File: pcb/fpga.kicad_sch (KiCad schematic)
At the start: 0 parts

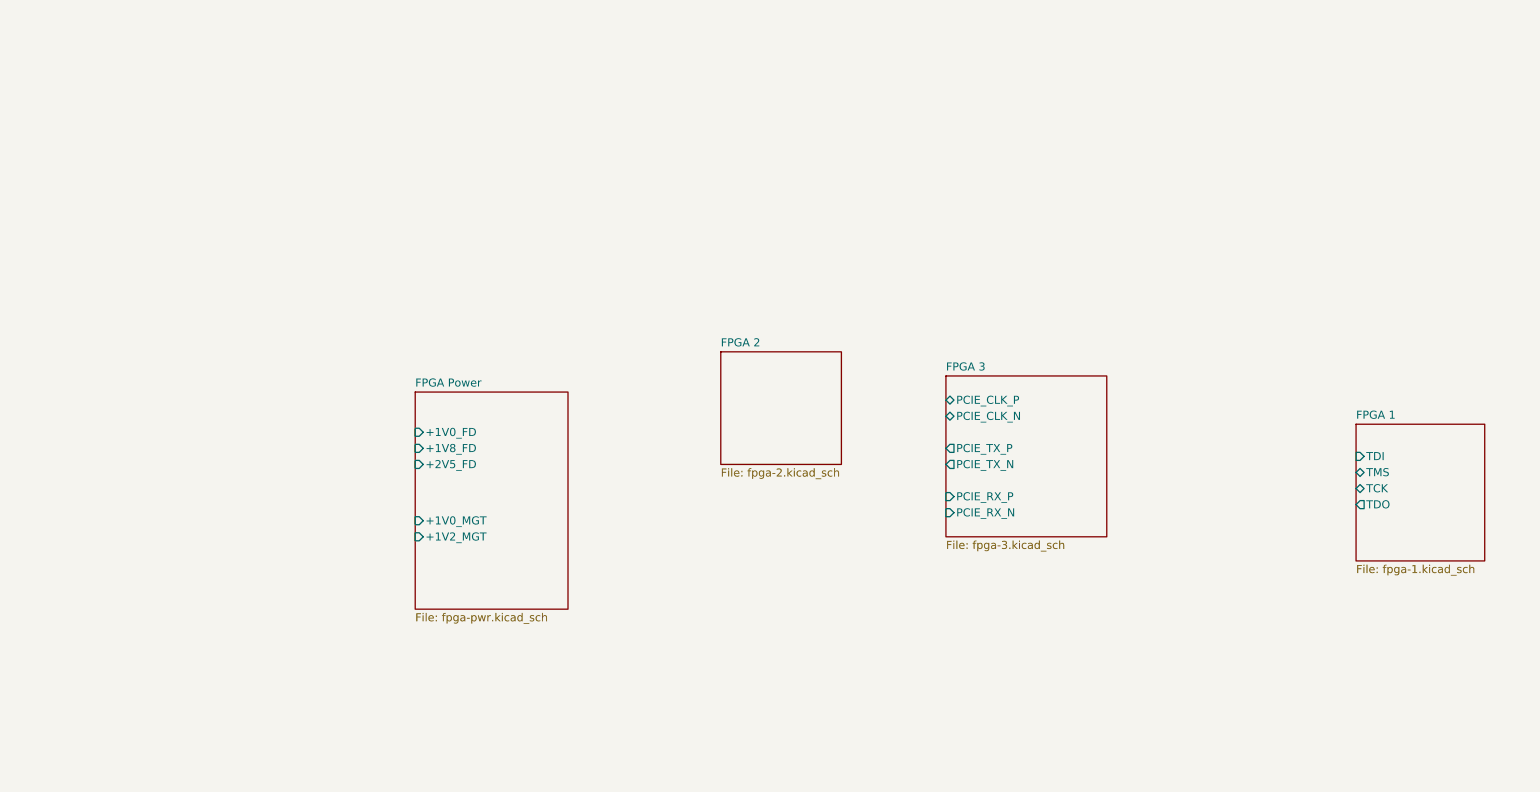
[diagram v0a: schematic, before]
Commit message: completed bus aliasing definitions
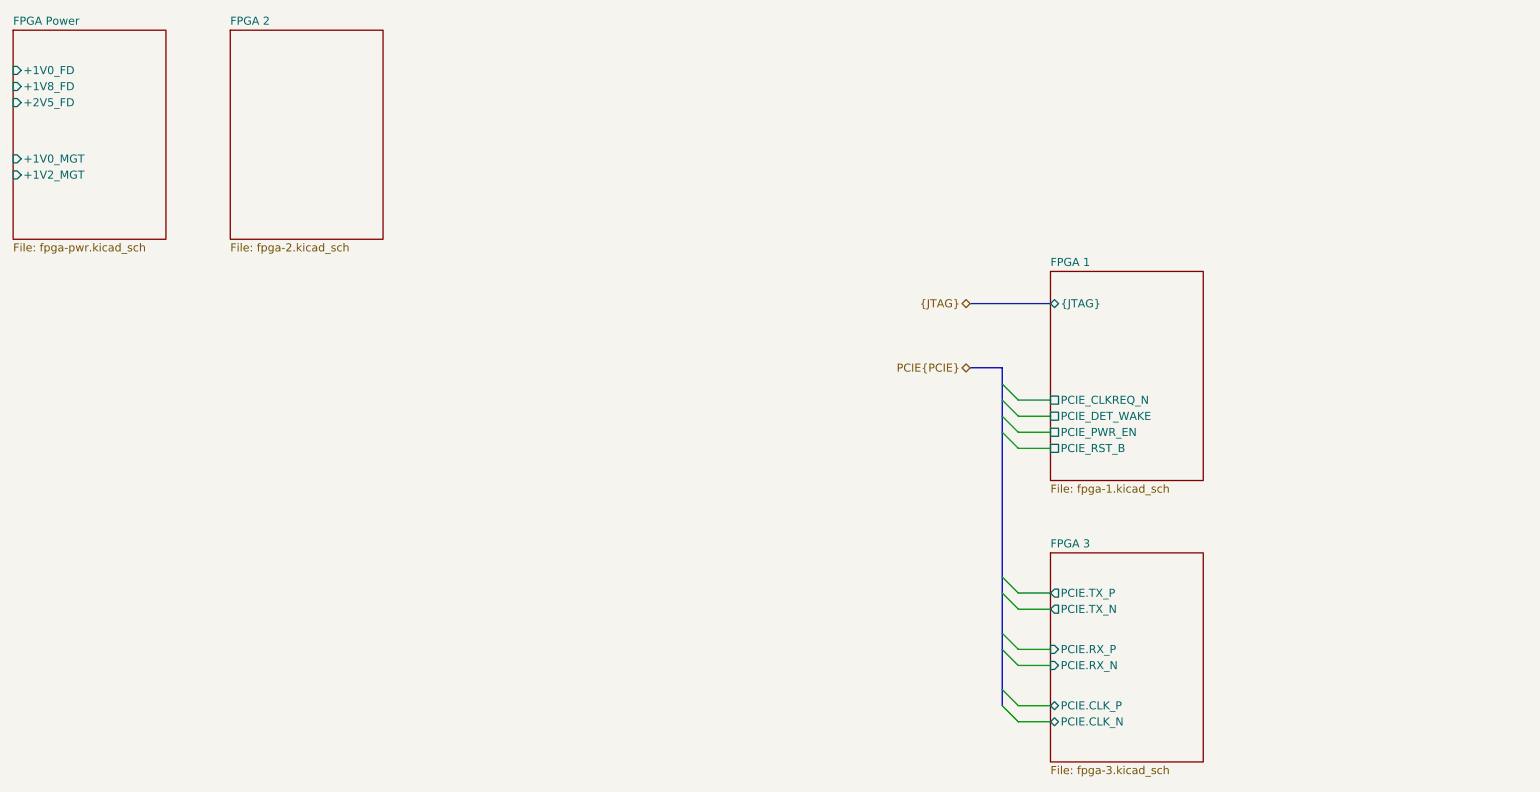
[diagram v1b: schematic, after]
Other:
- sheet FPGA 1 ports: added PCIE_CLKREQ_N, PCIE_DET_WAKE, PCIE_PWR_EN, PCIE_RST_B, {JTAG}; removed TCK, TDI, TDO, TMS
- sheet FPGA 3 ports: added PCIE.CLK_N, PCIE.CLK_P, PCIE.RX_N, PCIE.RX_P, PCIE.TX_N, PCIE.TX_P; removed PCIE_CLK_N, PCIE_CLK_P, PCIE_RX_N, PCIE_RX_P, PCIE_TX_N, PCIE_TX_P

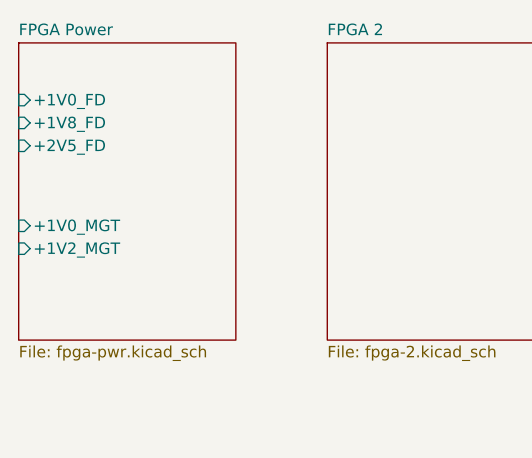
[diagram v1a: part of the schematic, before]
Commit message: updated sims, power hierarchy
added power flags to voltage buses, removed standard kicad "+3.3V" power flags and using standard kicad "power flag" in order to use hierarchical labels to visually show power paths
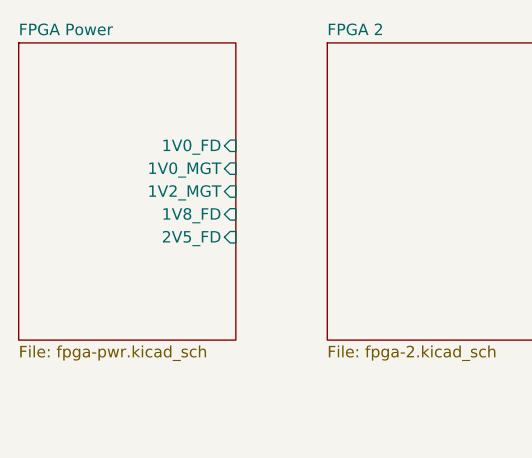
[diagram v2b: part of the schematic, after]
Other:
- sheet FPGA Power ports: added 1V0_FD, 1V0_MGT, 1V2_MGT, 1V8_FD, 2V5_FD; removed +1V0_FD, +1V0_MGT, +1V2_MGT, +1V8_FD, +2V5_FD
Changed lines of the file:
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@@
 			)
 		)
-		(pin "+1V0_FD" input
-			(at 19.05 25.4 180)
+		(pin "1V0_FD" input
+			(at 43.18 30.48 0)
 			(effects
 				(font
 					(size 1.27 1.27)
 				)
-				(justify left)
+				(justify right)
 			)
 		)
-		(pin "+1V0_MGT" input
-			(at 19.05 39.37 180)
+		(pin "1V0_MGT" input
+			(at 43.18 33.02 0)
 			(effects
 				(font
 					(size 1.27 1.27)
 				)
-				(justify left)
+				(justify right)
 			)
 		)
-		(pin "+1V2_MGT" input
-			(at 19.05 41.91 180)
+		(pin "1V2_MGT" input
+			(at 43.18 35.56 0)
 			(effects
 				(font
 					(size 1.27 1.27)
 				)
-				(justify left)
+				(justify right)
 			)
 		)
-		(pin "+1V8_FD" input
-			(at 19.05 27.94 180)
+		(pin "1V8_FD" input
+			(at 43.18 38.1 0)
 			(effects
 				(font
 					(size 1.27 1.27)
 				)
-				(justify left)
+				(justify right)
 			)
 		)
-		(pin "+2V5_FD" input
-			(at 19.05 30.48 180)
+		(pin "2V5_FD" input
+			(at 43.18 40.64 0)
 			(effects
 				(font
 					(size 1.27 1.27)
 				)
-				(justify left)
+				(justify right)
 			)
 		)

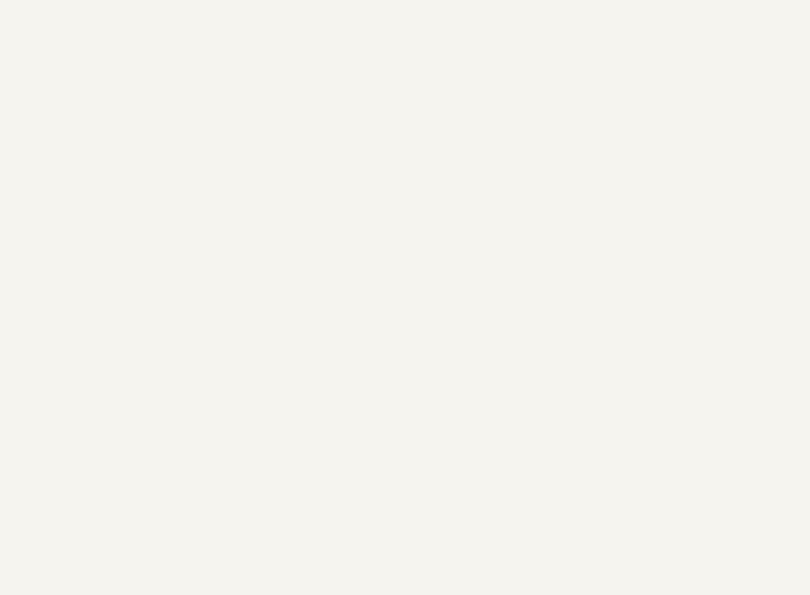
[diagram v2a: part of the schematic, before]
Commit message: restructured power hierarchy
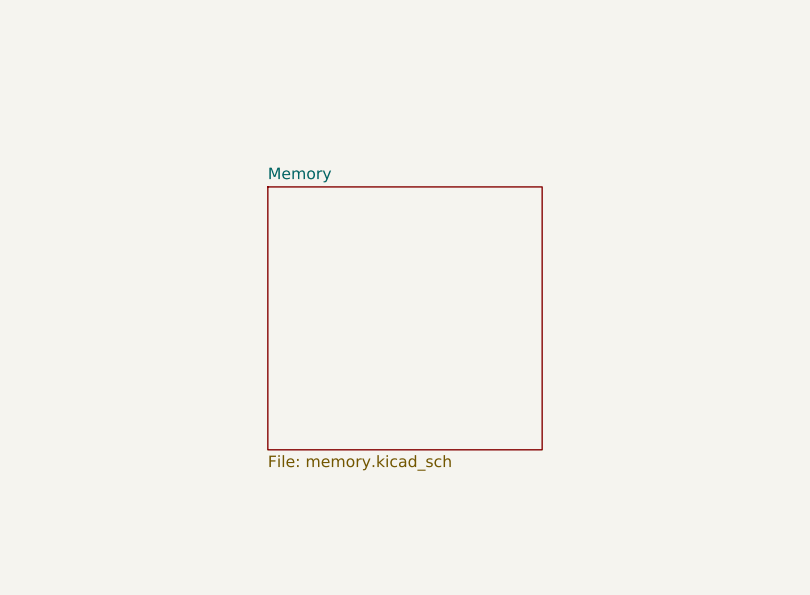
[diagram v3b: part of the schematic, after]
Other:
- added sheet Memory (memory.kicad_sch)
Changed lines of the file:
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@@
+	)
+	(sheet
+		(at 77.47 93.98)
+		(size 30.48 29.21)
+		(exclude_from_sim no)
+		(in_bom yes)
+		(on_board yes)
+		(dnp no)
+		(fields_autoplaced yes)
+		(stroke
+			(width 0.1524)
+			(type solid)
+		)
+		(fill
+			(color 0 0 0 0.0000)
+		)
+		(property "Sheetname" "Memory"
+			(at 77.47 93.2684 0)
+			(effects
+				(font
+					(size 1.27 1.27)
+				)
+				(justify left bottom)
+			)
+		)
+		(property "Sheetfile" "memory.kicad_sch"
+			(at 77.47 123.7746 0)
+			(effects
+				(font
+					(size 1.27 1.27)
+				)
+				(justify left top)
+			)
+		)
+		(instances
+			(project "RPi-HwAB-1"
+				(path "/e63e39d7-6ac0-4ffd-8aa3-1841a4541b55/59d21473-a004-4514-8090-fd93db818925"
+					(page "11")
+				)
+			)
+		)
 	)
 	(sheet

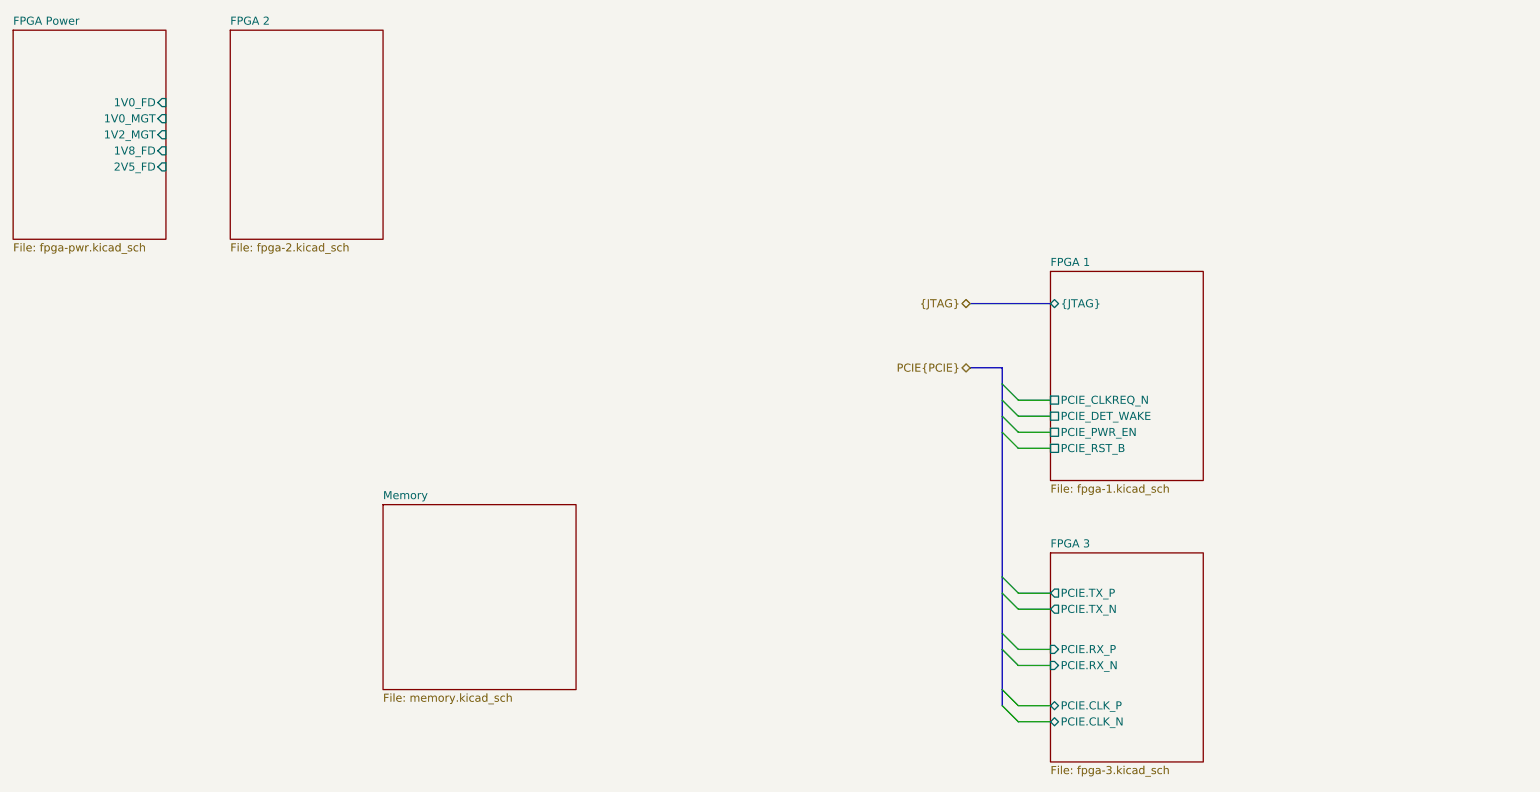
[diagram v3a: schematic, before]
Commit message: hierarchical current sense
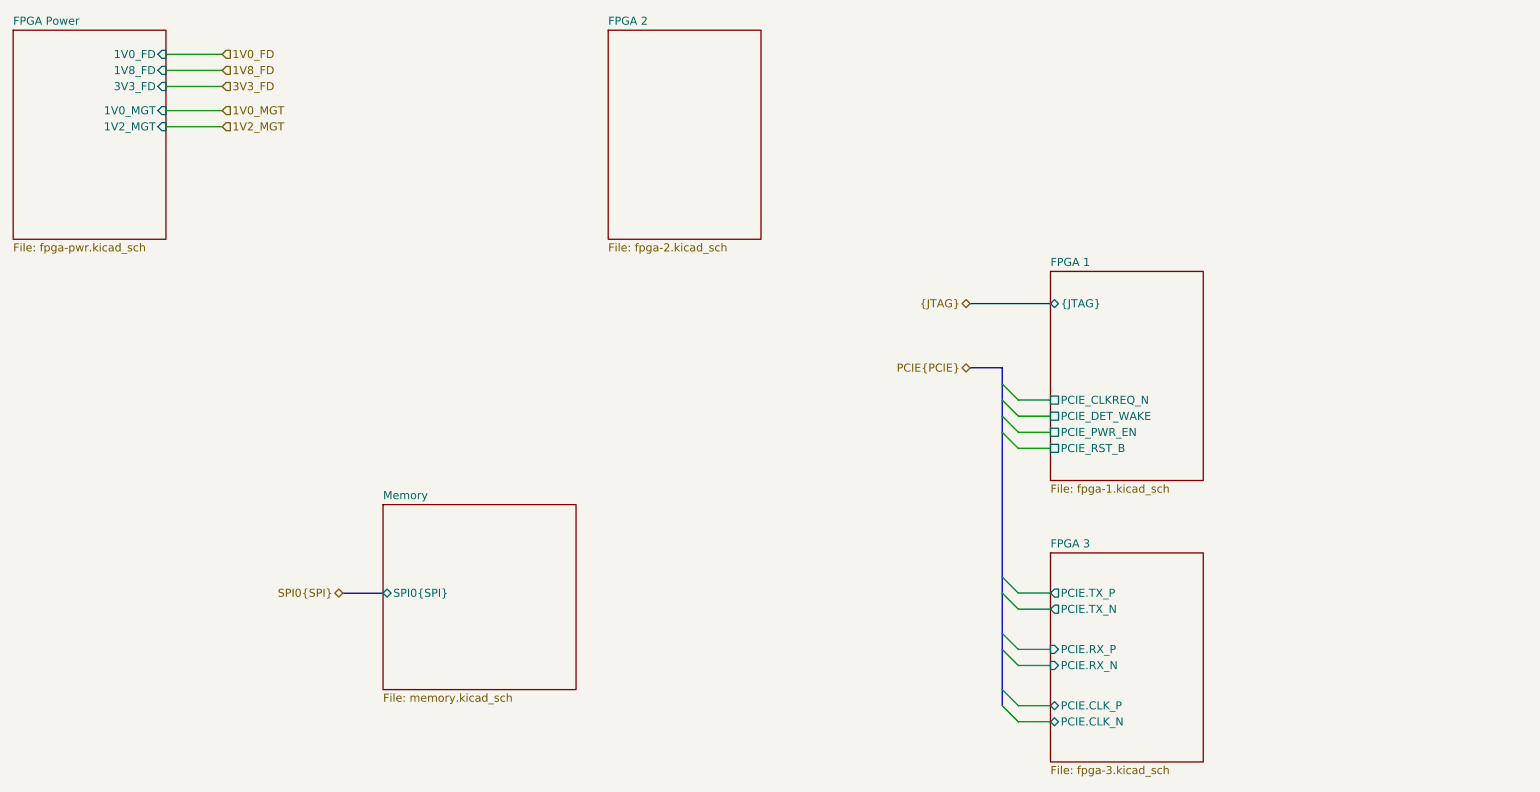
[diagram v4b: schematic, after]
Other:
- sheet FPGA Power ports: added 3V3_FD; removed 2V5_FD
- sheet Memory ports: added SPI0{SPI}; removed none
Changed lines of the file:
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@@
+		)
+	)
+	(wire
+		(pts
+			(xy 52.07 27.94) (xy 43.18 27.94)
+		)
+		(stroke
+			(width 0)
+			(type default)
+		)
+	)
+	(wire
+		(pts
+			(xy 52.07 22.86) (xy 43.18 22.86)
+		)
+		(stroke
+			(width 0)
+			(type default)
 		)
 	)
@@
 		)
 	)
+	(wire
+		(pts
+			(xy 52.07 31.75) (xy 43.18 31.75)
+		)
+		(stroke
+			(width 0)
+			(type default)
+		)
+	)
 	(bus
 		(pts
@@
 		)
 	)
+	(wire
+		(pts
+			(xy 52.07 25.4) (xy 43.18 25.4)
+		)
+		(stroke
+			(width 0)
+			(type default)
+		)
+	)
 	(bus
 		(pts
@@
 		(pts
 			(xy 177.8 77.47) (xy 182.88 77.47)
+		)
+		(stroke
+			(width 0)
+			(type default)
+		)
+	)
+	(bus
+		(pts
+			(xy 71.12 107.95) (xy 77.47 107.95)
+		)
+		(stroke
+			(width 0)
+			(type default)
+		)
+	)
+	(wire
+		(pts
+			(xy 52.07 34.29) (xy 43.18 34.29)
 		)
 		(stroke
@@
 		)
 	)
+	(hierarchical_label "1V0_MGT"
+		(shape input)
+		(at 52.07 31.75 0)
+		(effects
+			(font
+				(size 1.27 1.27)
+			)
+			(justify left)
+		)
+	)
+	(hierarchical_label "1V2_MGT"
+		(shape input)
+		(at 52.07 34.29 0)
+		(effects
+			(font
+				(size 1.27 1.27)
+			)
+			(justify left)
+		)
+	)
+	(hierarchical_label "1V0_FD"
+		(shape input)
+		(at 52.07 22.86 0)
+		(effects
+			(font
+				(size 1.27 1.27)
+			)
+			(justify left)
+		)
+	)
+	(hierarchical_label "1V8_FD"
+		(shape input)
+		(at 52.07 25.4 0)
+		(effects
+			(font
+				(size 1.27 1.27)
+			)
+			(justify left)
+		)
+	)
 	(hierarchical_label "PCIE{PCIE}"
 		(shape bidirectional)
@@
 			)
 			(justify right)
+		)
+	)
+	(hierarchical_label "SPI0{SPI}"
+		(shape bidirectional)
+		(at 71.12 107.95 180)
+		(effects
+			(font
+				(size 1.27 1.27)
+			)
+			(justify right)
+		)
+	)
+	(hierarchical_label "3V3_FD"
+		(shape input)
+		(at 52.07 27.94 0)
+		(effects
+			(font
+				(size 1.27 1.27)
+			)
+			(justify left)
 		)
 	)
@@
 		)
 		(pin "1V0_FD" input
-			(at 43.18 30.48 0)
+			(at 43.18 22.86 0)
 			(effects
 				(font
@@
 		)
 		(pin "1V0_MGT" input
-			(at 43.18 33.02 0)
+			(at 43.18 31.75 0)
 			(effects
 				(font
@@
 		)
 		(pin "1V2_MGT" input
-			(at 43.18 35.56 0)
+			(at 43.18 34.29 0)
 			(effects
 				(font
@@
 		)
 		(pin "1V8_FD" input
-			(at 43.18 38.1 0)
+			(at 43.18 25.4 0)
 			(effects
 				(font
@@
 			)
 		)
-		(pin "2V5_FD" input
-			(at 43.18 40.64 0)
+		(pin "3V3_FD" input
+			(at 43.18 27.94 0)
 			(effects
 				(font
@@
 			)
 		)
+		(pin "SPI0{SPI}" bidirectional
+			(at 77.47 107.95 180)
+			(effects
+				(font
+					(size 1.27 1.27)
+				)
+				(justify left)
+			)
+		)
 		(instances
 			(project "RPi-HwAB-1"
@@
 	)
 	(sheet
-		(at 53.34 19.05)
+		(at 113.03 19.05)
 		(size 24.13 33.02)
 		(exclude_from_sim no)
@@
 		)
 		(property "Sheetname" "FPGA 2"
-			(at 53.34 18.3384 0)
+			(at 113.03 18.3384 0)
 			(effects
 				(font
@@
 		)
 		(property "Sheetfile" "fpga-2.kicad_sch"
-			(at 53.34 52.6546 0)
-			(effects
-				(font
+			(at 113.03 52.6546 0)
+			(effects
+				(font
